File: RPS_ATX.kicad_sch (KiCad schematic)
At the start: 14 parts, among them J1 IN, U2 LM358, U3 L7815, U4 LM358, U6 AD586

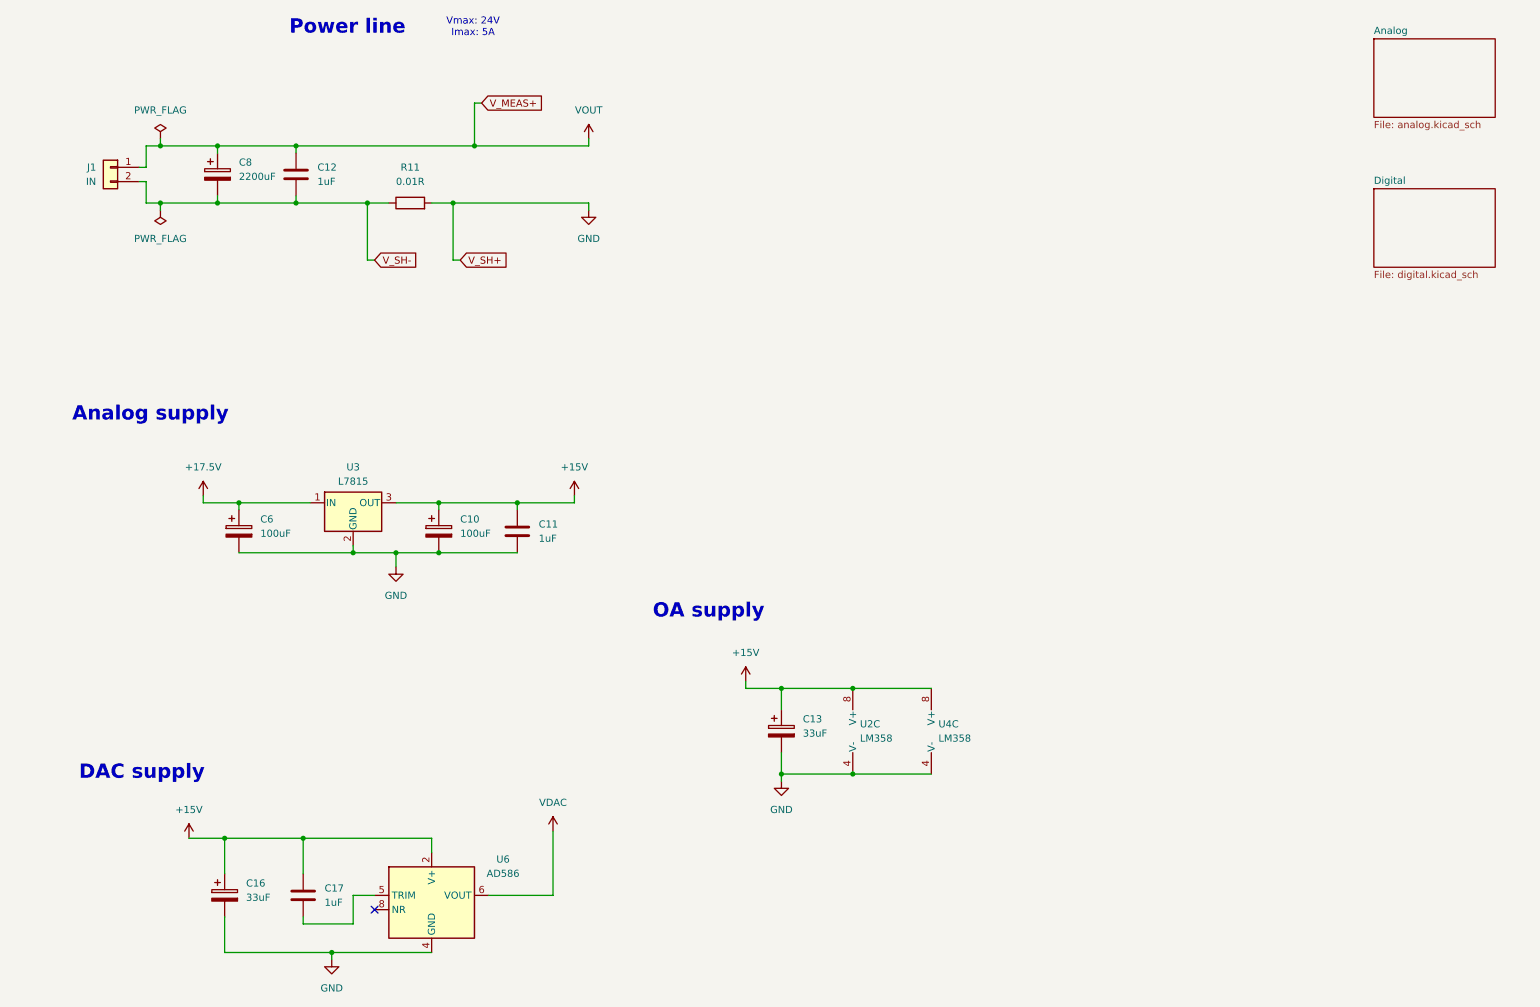
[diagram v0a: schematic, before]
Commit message: added: RC calculation,connectors Vin/Vmeas
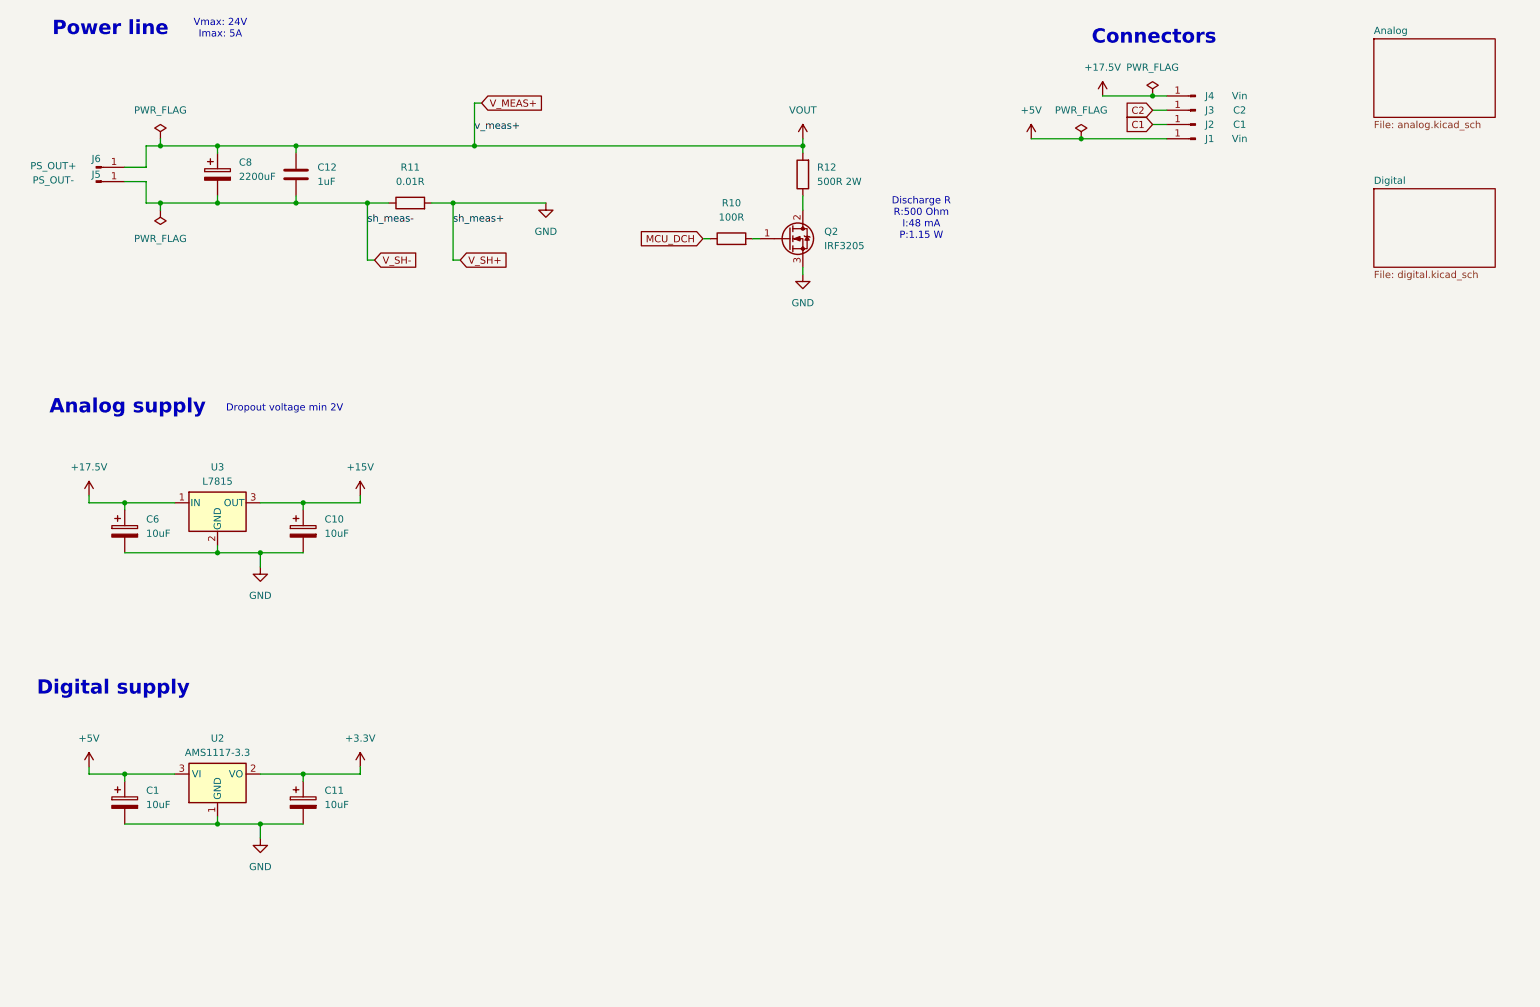
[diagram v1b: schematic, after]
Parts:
- removed C11: 1uF, symbol Device:C
- removed C13: 33uF, symbol Device:C_Polarized
- removed C16: 33uF, Capacitor_THT:CP_Radial_D7.5mm_P2.50mm, symbol Device:C_Polarized
- removed C17: 1uF, Capacitor_THT:C_Disc_D4.3mm_W1.9mm_P5.00mm, symbol Device:C
- removed J1: IN, symbol Connector_Generic:Conn_01x02
- removed U2, U4: LM358, symbol Amplifier_Operational:LM358
- removed U6: AD586, Package_DIP:DIP-8_W10.16mm, symbol Reference_Voltage:AD586
- added C1, C11: 10uF, symbol Device:C_Polarized
- added J1, J4: Vin, Connector_PinHeader_2.54mm:PinHeader_1x01_P2.54mm_Vertical, symbol Connector:Conn_01x01_Pin
- added J2: C1, Connector_PinHeader_2.54mm:PinHeader_1x01_P2.54mm_Vertical, symbol Connector:Conn_01x01_Pin
- added J3: C2, Connector_PinHeader_2.54mm:PinHeader_1x01_P2.54mm_Vertical, symbol Connector:Conn_01x01_Pin
- added J5: PS_OUT-, Connector_PinHeader_2.54mm:PinHeader_1x01_P2.54mm_Vertical, symbol Connector:Conn_01x01_Pin
- added J6: PS_OUT+, Connector_PinHeader_2.54mm:PinHeader_1x01_P2.54mm_Vertical, symbol Connector:Conn_01x01_Pin
- added Q2: IRF3205, Package_TO_SOT_THT:TO-220-3_Vertical, symbol Transistor_FET:IRF3205
- added R10: 100R, symbol Device:R
- added R12: 500R 2W, symbol Device:R
- added U2: AMS1117-3.3, Package_TO_SOT_SMD:SOT-223-3_TabPin2, symbol Regulator_Linear:AMS1117-3.3
- C10, C6: value 100uF -> 10uF
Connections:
- net +17.5V: now also J4.1 (Pin_1)
- net GND: now also C1.2, C11.2, Q2.3 (S), U2.1 (GND)
- net VOUT: now also J6.1 (Pin_1), R12.2
- net V_SH-: now also J5.1 (Pin_1)
- new net: Q2.1 (G), R10.2
- new net: Q2.2 (D), R12.1
- new net +3.3V: C11.1, U2.2 (VO)
- new net +5V: C1.1, J1.1 (Pin_1), U2.3 (VI)
- new net C1: J2.1 (Pin_1)
- new net C2: J3.1 (Pin_1)
- new net MCU_DCH: R10.1
- no-connect marks 1 -> 0
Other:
- note added: "Connectors"
- note added: "Digital supply"
- note added: "Discharge R R:500 Ohm I:48 mA P:1.15 W"
- note added: "Dropout voltage min 2V"
- note removed: "DAC supply"
- note removed: "OA supply"
- moved on the sheet: C10, C6, U3

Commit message: new OpAmp, new RC calc, G431 added
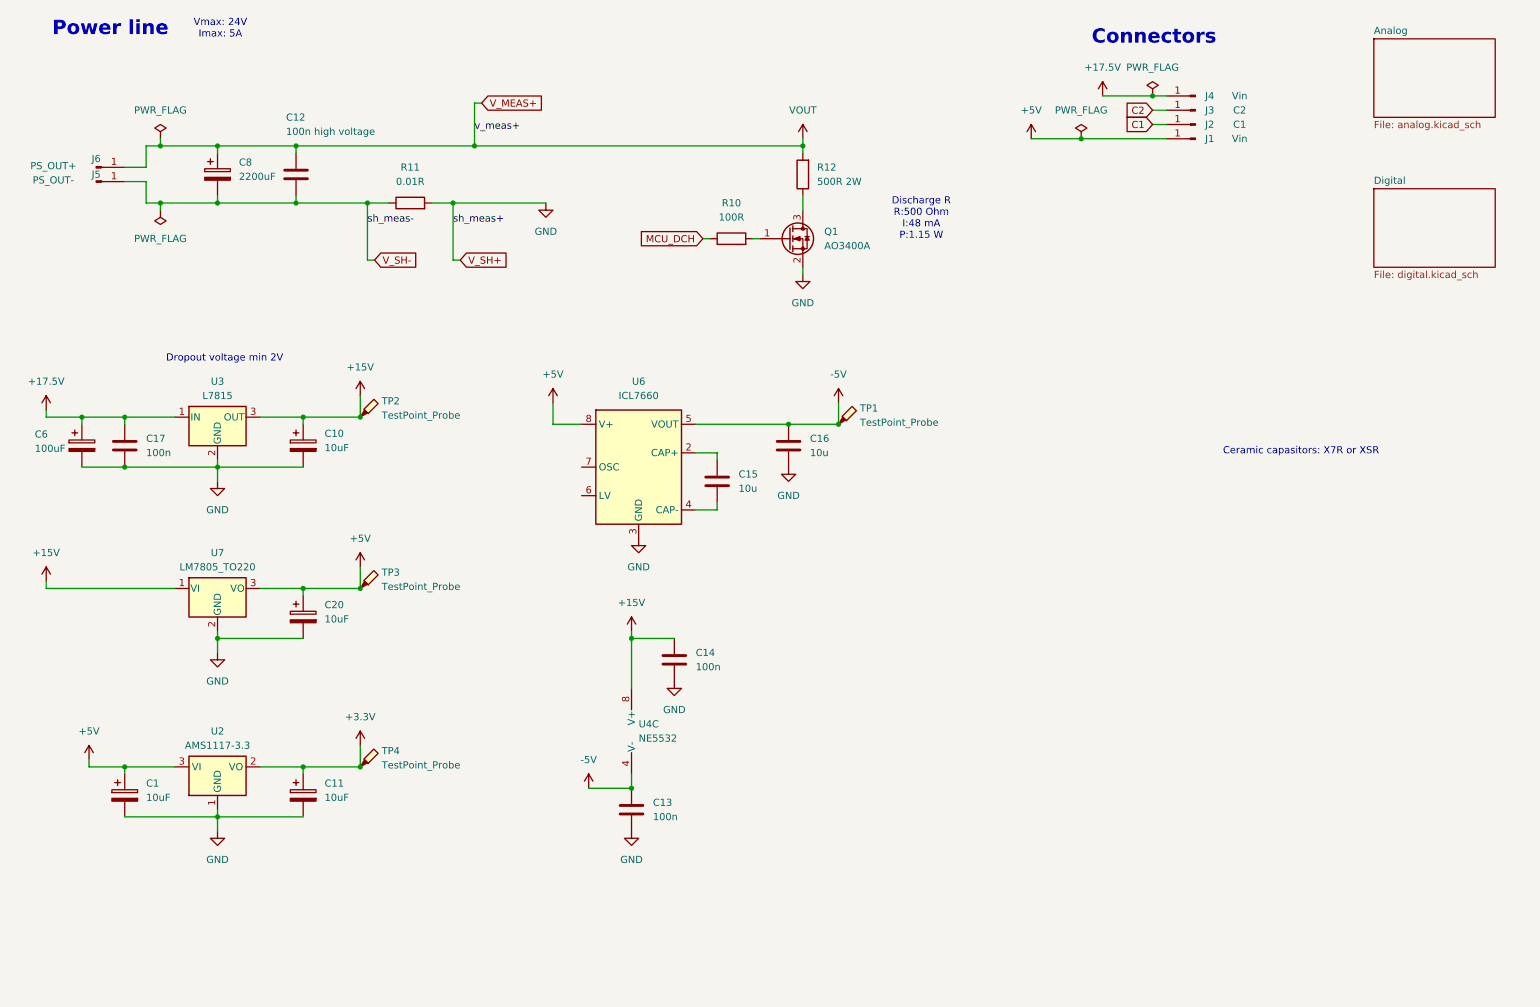
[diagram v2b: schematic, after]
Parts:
- removed Q2: IRF3205, Package_TO_SOT_THT:TO-220-3_Vertical, symbol Transistor_FET:IRF3205
- added C13, C14, C17: 100n, symbol Device:C
- added C15, C16: 10u, symbol Device:C
- added C20: 10uF, symbol Device:C_Polarized
- added Q1: AO3400A, Package_TO_SOT_SMD:SOT-23, symbol Transistor_FET:AO3400A
- added TP1, TP2, TP3, TP4: TestPoint_Probe, symbol Connector:TestPoint_Probe
- added U4: NE5532, Package_SO:SOIC-8_3.9x4.9mm_P1.27mm, symbol Amplifier_Operational:NE5532
- added U6: ICL7660, Package_DIP:DIP-8_W7.62mm, symbol Regulator_SwitchedCapacitor:ICL7660
- added U7: LM7805_TO220, Package_TO_SOT_THT:TO-220-3_Vertical, symbol Regulator_Linear:LM7805_TO220
- C12: value 1uF -> 100n high voltage
- C6: value 10uF -> 100uF
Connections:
- net +15V: now also C14.1, TP2.1, U4.8 (V+), U7.1 (VI)
- net +17.5V: now also C17.1
- net +3.3V: now also TP4.1
- net +5V: now also C20.1, TP3.1, U6.8 (V+), U7.3 (VO)
- net GND: now also C13.2, C14.2, C16.2, C17.2, C20.2, Q1.2 (S), U6.3 (GND), U7.2 (GND)
- net at R10.2: now also Q1.1 (G)
- net at R12.1: now also Q1.3 (D)
- new net: C15.1, U6.2 (CAP+)
- new net: C15.2, U6.4 (CAP-)
- new net -5V: C13.1, C16.1, TP1.1, U4.4 (V-), U6.5 (VOUT)
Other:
- note added: "Ceramic capasitors: X7R or XSR"
- note removed: "Analog supply"
- note removed: "Digital supply"
- moved on the sheet: C1, C10, C11, C6, U2, U3

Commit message: MCU analog perephery, TL494 FB wiring
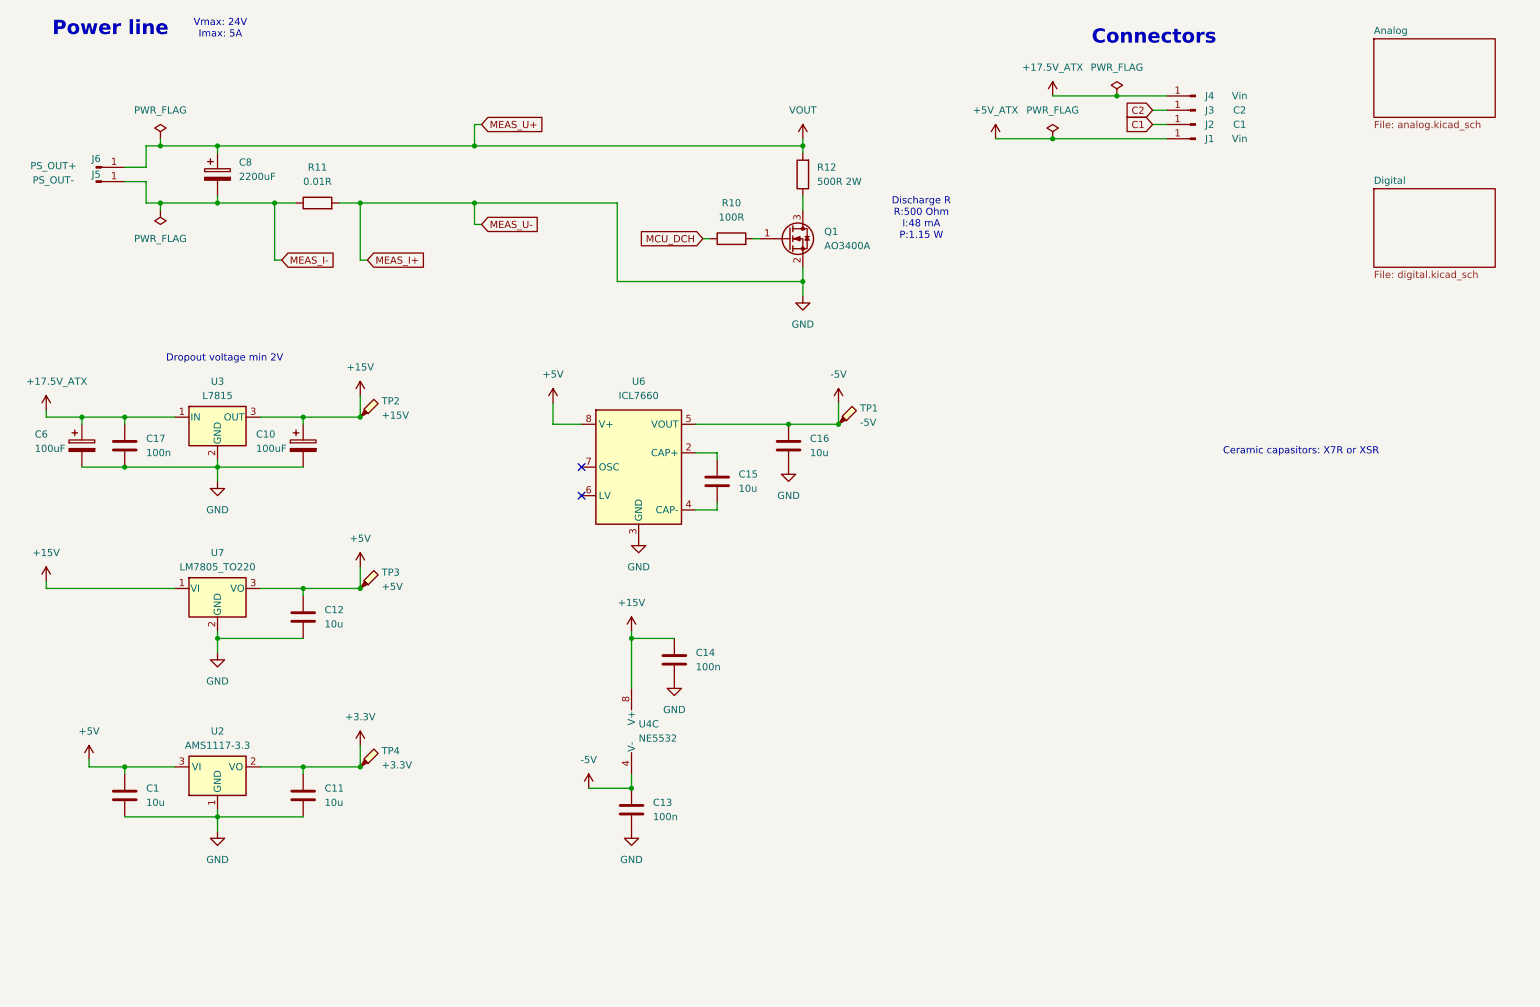
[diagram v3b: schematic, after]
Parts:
- removed C1, C11, C20: 10uF, symbol Device:C_Polarized
- added C1, C11: 10u, symbol Device:C
- C10: value 10uF -> 100uF
- C12: value 100n high voltage -> 10u
- TP1: value TestPoint_Probe -> -5V
- TP2: value TestPoint_Probe -> +15V
- TP3: value TestPoint_Probe -> +5V
- TP4: value TestPoint_Probe -> +3.3V
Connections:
- net +3.3V: now also C11.1
- net +5V: now also C12.1, C1.1; no longer J1.1 (Pin_1)
- net GND: now also C12.2, C1.2, C11.2
- net VOUT: no longer C12.1
- net +17.5V renamed +17.5V_ATX
- net V_SH- renamed MEAS_I-
- net MEAS_I-: no longer C12.2
- new net +5V_ATX: J1.1 (Pin_1)
- no-connect marks 0 -> 2
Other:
- moved on the sheet: R11

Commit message: assign footprints
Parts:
- added J7: RPS_OUT+, Connector_Wire:SolderWire-4sqmm_1x01_D3mm_OD6mm, symbol Connector:Conn_01x01_Pin
- added J9: RPS_OUT-, Connector_Wire:SolderWire-4sqmm_1x01_D3mm_OD6mm, symbol Connector:Conn_01x01_Pin
- C1, C11, C12, C15, C16: footprint (none) -> Capacitor_SMD:C_1206_3216Metric_Pad1.33x1.80mm_HandSolder
- C10, C6: footprint (none) -> Capacitor_SMD:CP_Elec_6.3x5.4_Nichicon
- C13, C14, C17: footprint (none) -> Capacitor_SMD:C_0805_2012Metric_Pad1.18x1.45mm_HandSolder
- C8: footprint (none) -> Capacitor_THT:CP_Radial_D18.0mm_P7.50mm
- J1: value Vin -> 5V
- J4: value Vin -> 17.5V
- J5, J6: footprint Connector_PinHeader_2.54mm:PinHeader_1x01_P2.54mm_Vertical -> Connector_Wire:SolderWire-2sqmm_1x01_D2mm_OD3.9mm
- R10: footprint (none) -> Resistor_SMD:R_1206_3216Metric_Pad1.30x1.75mm_HandSolder
- R11: footprint (none) -> my lib:Resistor_Shunt_L10_D3.7
- R12: value 500R 2W -> 510R 2W; footprint (none) -> Resistor_THT:R_Axial_DIN0414_L11.9mm_D4.5mm_P5.08mm_Vertical
- TP1, TP2, TP3, TP4: footprint (none) -> TestPoint:TestPoint_Pad_D2.0mm
- U3: footprint (none) -> Package_TO_SOT_SMD:TO-252-3_TabPin2
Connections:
- net MEAS_I- is gone; now on net GND: C8.2, J5.1 (Pin_1), R11.1
- net GND: no longer Q1.2 (S), R11.2
- net VOUT: now also J9.1 (Pin_1)
- new net MEAS_I+: J7.1 (Pin_1), Q1.2 (S), R11.2
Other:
- moved on the sheet: Q1, R10, R12
